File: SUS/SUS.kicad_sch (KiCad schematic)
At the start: 64 parts, among them J1 ESP32_Connector_0, J2 ESP32_Connector_1, J3 I2C, J4 I2C, J5 I2C, J6 ADC, J7 WS, U1 TJA1051T, U2 ADS8320EB_250, U3 ICM-42688-P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

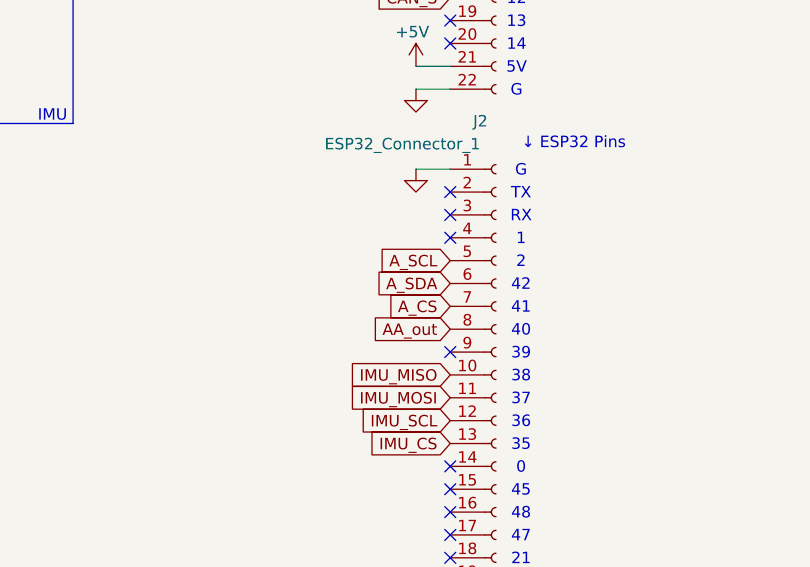
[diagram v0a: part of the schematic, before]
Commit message: Changed ESP32 analog pin
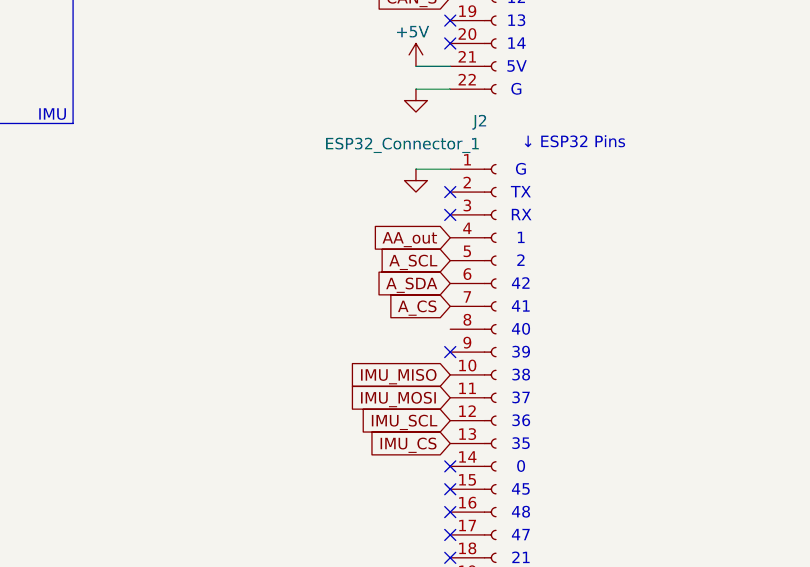
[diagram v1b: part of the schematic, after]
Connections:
- net AA_out: now also J2.4 (Pin_4); no longer J2.8 (Pin_8)
- no-connect marks 24 -> 23
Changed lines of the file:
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@@
-	)
-	(no_connect
-		(at 234.95 96.52)
 	)
 	(no_connect
@@
 	)
 	(no_connect
-		(at 234.95 93.98)
-	)
-	(no_connect
 		(at 234.95 129.54)
 	)
@@
 	(no_connect
 		(at 234.95 57.15)
+	)
+	(no_connect
+		(at 234.95 93.98)
 	)
 	(no_connect
@@
 	(global_label "AA_out"
 		(shape input)
-		(at 234.95 106.68 180)
+		(at 234.95 96.52 180)
 		(fields_autoplaced yes)
 		(effects
@@
 		)
 		(property "Intersheetrefs" "${INTERSHEET_REFS}"
-			(at 225.7963 106.68 0)
+			(at 225.7963 96.52 0)
 			(effects
 				(font

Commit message: Minor fixes & generated fabrication files
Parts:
- C1, C2, C3, C4, C5, J1, J2, J3, J4, J5, J6, J7, R1, R2, U1, U2, U4, U5, U6: now not fitted
- C10, C11, C12, C13, C14, C15, C16, C17, C18, C19, C20, C21, C22, C23, C24, C25, C6, C7, C8, C9: LCSC PN (none) -> C76941
- R10, R11, R12, R13, R14, R15, R16, R17, R18, R19, R20, R21, R22, R3, R4, R5, R6, R7, R8, R9: JLCpart# C2906988 -> (none); LCSC PN (none) -> C270365
- U3: LCSC PN (none) -> C1850418

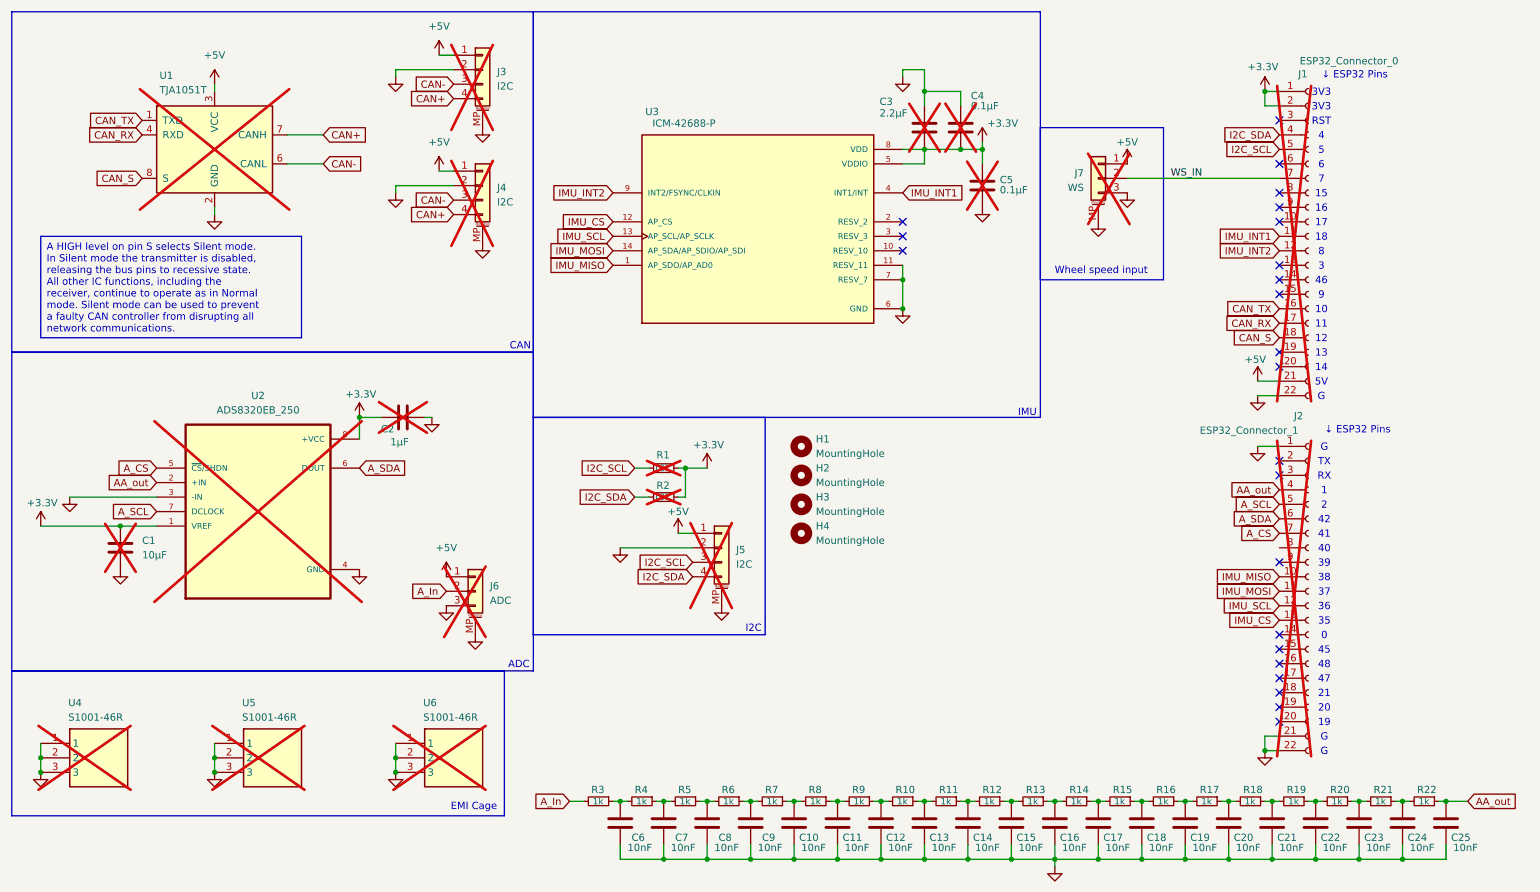
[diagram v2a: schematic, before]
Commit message: Updated trace names & README.md
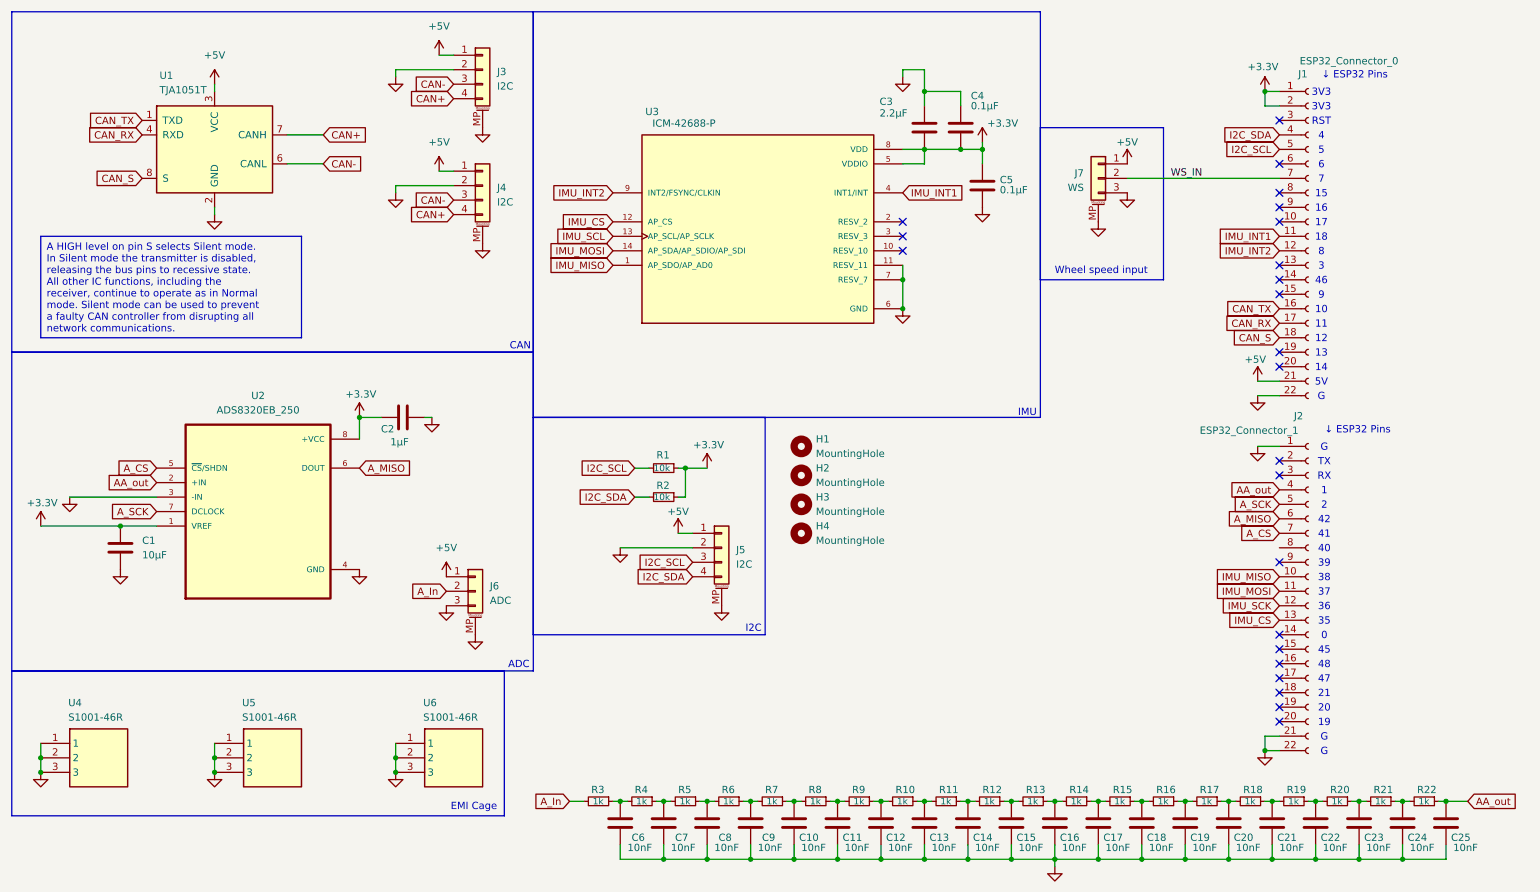
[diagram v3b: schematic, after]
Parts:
- C1, C2, C3, C4, C5, J1, J2, J3, J4, J5, J6, J7, R1, R2, U1, U2, U4, U5, U6: now fitted
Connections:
- net IMU_SCL: no longer J2.12 (Pin_12)
- net A_SCL renamed A_SCK
- net A_SDA renamed A_MISO
- new net IMU_SCK: J2.12 (Pin_12)
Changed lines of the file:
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@@
 		)
 	)
-	(global_label "A_SCL"
+	(global_label "A_SCK"
 		(shape input)
 		(at 38.1 100.33 180)
@@
 		)
 		(property "Intersheetrefs" "${INTERSHEET_REFS}"
-			(at 29.551 100.33 0)
+			(at 29.3091 100.33 0)
 			(effects
 				(font
@@
 		)
 	)
-	(global_label "A_SDA"
+	(global_label "A_MISO"
 		(shape input)
 		(at 234.95 101.6 180)
@@
 		)
 		(property "Intersheetrefs" "${INTERSHEET_REFS}"
-			(at 226.3405 101.6 0)
+			(at 225.3124 101.6 0)
 			(effects
 				(font
@@
 		)
 	)
-	(global_label "IMU_SCL"
+	(global_label "IMU_SCK"
 		(shape input)
 		(at 234.95 116.84 180)
@@
 		)
 		(property "Intersheetrefs" "${INTERSHEET_REFS}"
-			(at 224.1029 116.84 0)
+			(at 223.861 116.84 0)
 			(effects
 				(font
@@
 		)
 	)
-	(global_label "A_SCL"
+	(global_label "A_SCK"
 		(shape input)
 		(at 234.95 99.06 180)
@@
 		)
 		(property "Intersheetrefs" "${INTERSHEET_REFS}"
-			(at 226.401 99.06 0)
+			(at 226.1591 99.06 0)
 			(effects
 				(font
@@
 		)
 	)
-	(global_label "A_SDA"
+	(global_label "A_MISO"
 		(shape input)
 		(at 73.66 92.71 0)
@@
 		)
 		(property "Intersheetrefs" "${INTERSHEET_REFS}"
-			(at 82.2695 92.71 0)
+			(at 83.2976 92.71 0)
 			(effects
 				(font
@@
 		(in_bom yes)
 		(on_board yes)
-		(dnp yes)
+		(dnp no)
 		(property "Reference" "J1"
 			(at 238.252 23.622 0)
@@
 		(in_bom yes)
 		(on_board yes)
-		(dnp yes)
+		(dnp no)
 		(fields_autoplaced yes)
 		(property "Reference" "J6"
@@
 		(in_bom yes)
 		(on_board yes)
-		(dnp yes)
+		(dnp no)
 		(property "Reference" "J7"
 			(at 200.66 40.9955 0)
@@
 		(in_bom yes)
 		(on_board yes)
-		(dnp yes)
+		(dnp no)
 		(property "Reference" "R2"
 			(at 125.73 95.758 90)
@@
 		(in_bom yes)
 		(on_board yes)
-		(dnp yes)
+		(dnp no)
 		(fields_autoplaced yes)
 		(property "Reference" "J3"
@@
 		(in_bom yes)
 		(on_board yes)
-		(dnp yes)
+		(dnp no)
 		(property "Reference" "U4"
 			(at 22.606 133.858 0)
@@
 		(in_bom yes)
 		(on_board yes)
-		(dnp yes)
+		(dnp no)
 		(property "Reference" "U5"
 			(at 53.086 133.858 0)
@@
 		(in_bom yes)
 		(on_board yes)
-		(dnp yes)
+		(dnp no)
 		(fields_autoplaced yes)
 		(property "Reference" "J5"
@@
 		(in_bom yes)
 		(on_board yes)
-		(dnp yes)
+		(dnp no)
 		(property "Reference" "C5"
 			(at 185.928 42.164 0)
@@
 		(in_bom yes)
 		(on_board yes)
-		(dnp yes)
+		(dnp no)
 		(property "Reference" "C3"
 			(at 164.846 28.448 0)
@@
 		(in_bom yes)
 		(on_board yes)
-		(dnp yes)
+		(dnp no)
 		(fields_autoplaced yes)
 		(property "Reference" "C1"
@@
 		(in_bom yes)
 		(on_board yes)
-		(dnp yes)
+		(dnp no)
 		(property "Reference" "C4"
 			(at 180.848 27.432 0)
@@
 		(in_bom yes)
 		(on_board yes)
-		(dnp yes)
+		(dnp no)
 		(property "Reference" "J2"
 			(at 237.49 83.566 0)
@@
 		(in_bom yes)
 		(on_board yes)
-		(dnp yes)
+		(dnp no)
 		(property "Reference" "U1"
 			(at 38.608 23.876 0)
@@
 		(in_bom yes)
 		(on_board yes)
-		(dnp yes)
+		(dnp no)
 		(property "Reference" "U6"
 			(at 84.836 133.858 0)
@@
 		(in_bom yes)
 		(on_board yes)
-		(dnp yes)
+		(dnp no)
 		(property "Reference" "R1"
 			(at 125.73 90.424 90)
@@
 		(in_bom yes)
 		(on_board yes)
-		(dnp yes)
+		(dnp no)
 		(fields_autoplaced yes)
 		(property "Reference" "U2"
@@
 		(in_bom yes)
 		(on_board yes)
-		(dnp yes)
+		(dnp no)
 		(fields_autoplaced yes)
 		(property "Reference" "J4"
@@
 		(in_bom yes)
 		(on_board yes)
-		(dnp yes)
+		(dnp no)
 		(property "Reference" "C2"
 			(at 79.756 85.852 90)
